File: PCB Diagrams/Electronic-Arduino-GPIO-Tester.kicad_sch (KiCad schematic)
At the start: 49 parts, among them J1 POWER, J2 Conn_01x02, J3 Conn_01x12, J4 Conn_01x08

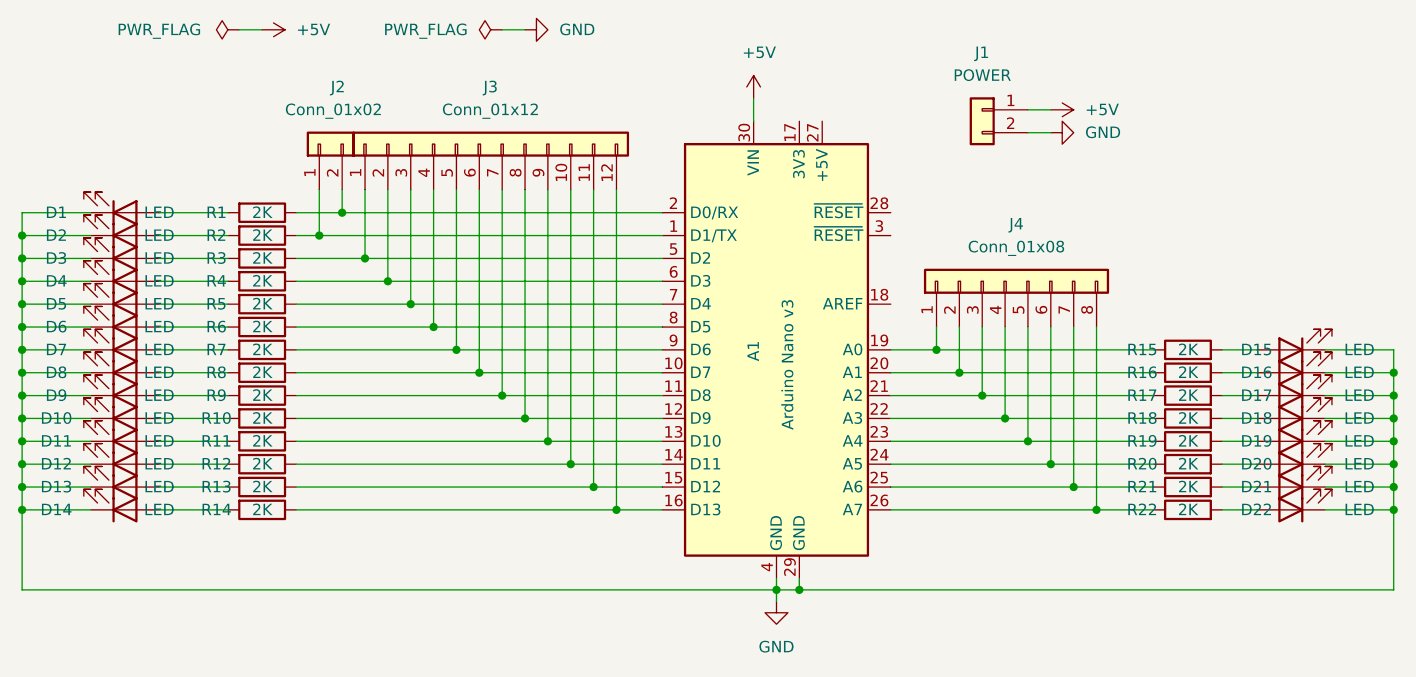
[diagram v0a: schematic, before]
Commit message: pcb size optimization
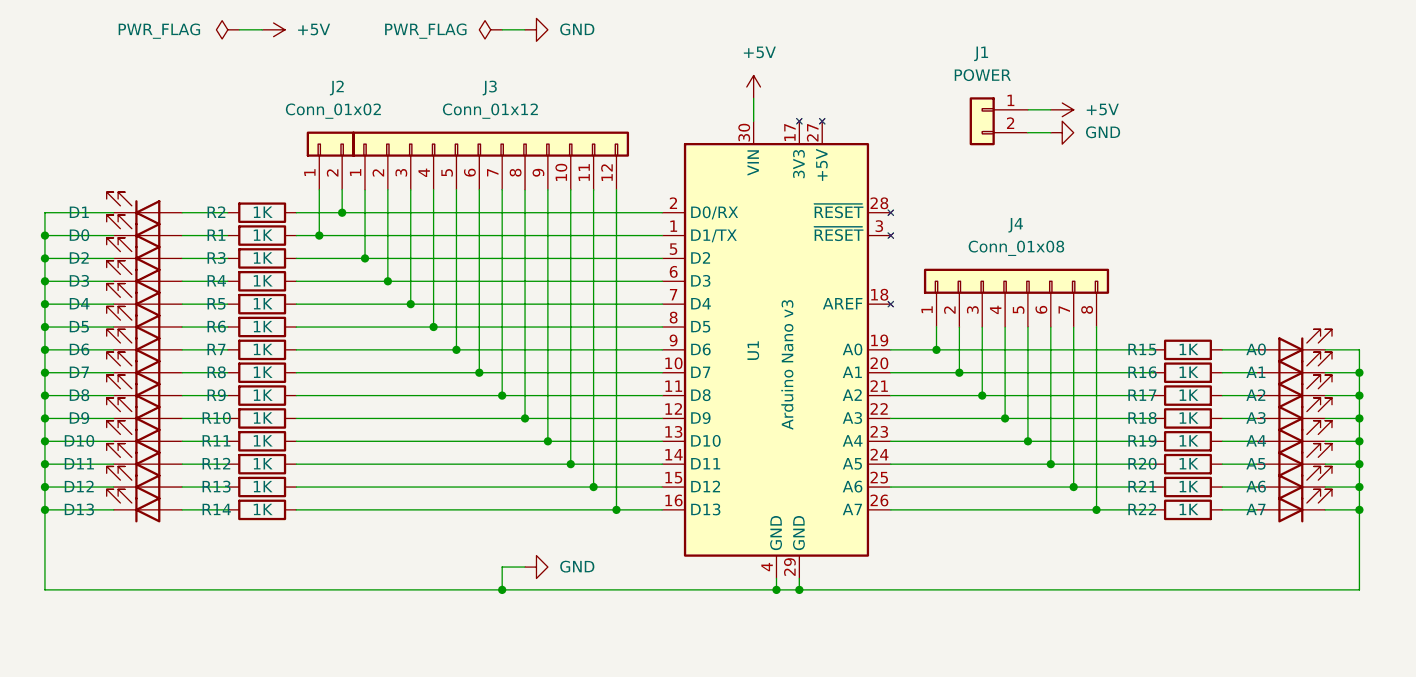
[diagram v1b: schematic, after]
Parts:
- A0: renamed from D15; footprint LED_THT:LED_D5.0mm -> LED_THT:LED_D3.0mm
- A1: renamed from D16; footprint LED_THT:LED_D5.0mm -> LED_THT:LED_D3.0mm
- A2: renamed from D17; footprint LED_THT:LED_D5.0mm -> LED_THT:LED_D3.0mm
- A3: renamed from D18; footprint LED_THT:LED_D5.0mm -> LED_THT:LED_D3.0mm
- A4: renamed from D19; footprint LED_THT:LED_D5.0mm -> LED_THT:LED_D3.0mm
- A5: renamed from D20; footprint LED_THT:LED_D5.0mm -> LED_THT:LED_D3.0mm
- A6: renamed from D21; footprint LED_THT:LED_D5.0mm -> LED_THT:LED_D3.0mm
- A7: renamed from D22; footprint LED_THT:LED_D5.0mm -> LED_THT:LED_D3.0mm
- D0: renamed from D2; footprint LED_THT:LED_D5.0mm -> LED_THT:LED_D3.0mm
- D1: footprint LED_THT:LED_D5.0mm -> LED_THT:LED_D3.0mm
- D10: renamed from D11; footprint LED_THT:LED_D5.0mm -> LED_THT:LED_D3.0mm
- D11: renamed from D12; footprint LED_THT:LED_D5.0mm -> LED_THT:LED_D3.0mm
- D12: renamed from D13; footprint LED_THT:LED_D5.0mm -> LED_THT:LED_D3.0mm
- D13: renamed from D14; footprint LED_THT:LED_D5.0mm -> LED_THT:LED_D3.0mm
- D2: renamed from D3; footprint LED_THT:LED_D5.0mm -> LED_THT:LED_D3.0mm
- D3: renamed from D4; footprint LED_THT:LED_D5.0mm -> LED_THT:LED_D3.0mm
- D4: renamed from D5; footprint LED_THT:LED_D5.0mm -> LED_THT:LED_D3.0mm
- D5: renamed from D6; footprint LED_THT:LED_D5.0mm -> LED_THT:LED_D3.0mm
- D6: renamed from D7; footprint LED_THT:LED_D5.0mm -> LED_THT:LED_D3.0mm
- D7: renamed from D8; footprint LED_THT:LED_D5.0mm -> LED_THT:LED_D3.0mm
- D8: renamed from D9; footprint LED_THT:LED_D5.0mm -> LED_THT:LED_D3.0mm
- D9: renamed from D10; footprint LED_THT:LED_D5.0mm -> LED_THT:LED_D3.0mm
- R1: renamed from R2; value 2K -> 1K; footprint Resistor_THT:R_Axial_DIN0207_L6.3mm_D2.5mm_P10.16mm_Horizontal -> Resistor_THT:R_Axial_DIN0207_L6.3mm_D2.5mm_P7.62mm_Horizontal
- R10, R11, R12, R13, R14, R15, R16, R17, R18, R19, R20, R21, R22, R3, R4, R5, R6, R7, R8, R9: value 2K -> 1K; footprint Resistor_THT:R_Axial_DIN0207_L6.3mm_D2.5mm_P10.16mm_Horizontal -> Resistor_THT:R_Axial_DIN0207_L6.3mm_D2.5mm_P7.62mm_Horizontal
- R2: renamed from R1; value 2K -> 1K; footprint Resistor_THT:R_Axial_DIN0207_L6.3mm_D2.5mm_P10.16mm_Horizontal -> Resistor_THT:R_Axial_DIN0207_L6.3mm_D2.5mm_P7.62mm_Horizontal
- renumbered A1 to U1
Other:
- moved on the sheet: D0, D1, D10, D11, D12, D13, D2, D3, D4, D5, D6, D7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
